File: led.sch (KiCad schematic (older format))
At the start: 2 parts

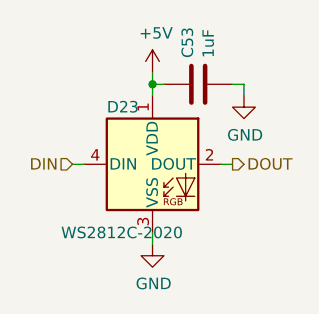
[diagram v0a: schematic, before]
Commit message: Place and route WS2812 LEDs
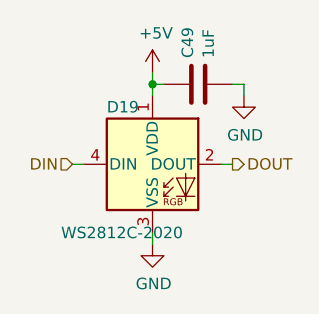
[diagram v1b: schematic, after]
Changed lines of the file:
@@
 $Descr A4 11693 8268
 encoding utf-8
-Sheet 22 23
+Sheet 19 17
 Title ""
 Date ""
@@
 AR Path="/62050786/62063495/6205F43D" Ref="D16"  Part="1"
 AR Path="/62050786/620637A1/6205F43D" Ref="D17"  Part="1"
-F 0 "D23" H 1800 2600 50  0000 L CNN
+F 0 "D19" H 1800 2600 50  0000 L CNN
 F 1 "WS2812C-2020" H 1600 2050 50  0000 L CNN
 F 2 "LED_RGB:LED_RGB_2020_WS2812C" H 2050 2050 50  0001 L TNN
@@
 AR Path="/62050786/62063495/6205F444" Ref="C46"  Part="1"
 AR Path="/62050786/620637A1/6205F444" Ref="C47"  Part="1"
-F 0 "C53" H 2315 2046 50  0000 L CNN
+F 0 "C49" H 2315 2046 50  0000 L CNN
 F 1 "1uF" H 2315 1955 50  0000 L CNN
 F 2 "Capacitor_SMD:C_0402_1005Metric" H 2238 1850 50  0001 C CNN
@@
 AR Path="/62050786/62063495/6205F44A" Ref="#PWR0164"  Part="1"
 AR Path="/62050786/620637A1/6205F44A" Ref="#PWR0167"  Part="1"
-F 0 "#PWR0185" H 2400 1800 50  0001 C CNN
+F 0 "#PWR0173" H 2400 1800 50  0001 C CNN
 F 1 "GND" H 2405 1877 50  0000 C CNN
 F 2 "" H 2400 2050 50  0001 C CNN
@@
 AR Path="/62050786/62063495/6205F452" Ref="#PWR0165"  Part="1"
 AR Path="/62050786/620637A1/6205F452" Ref="#PWR0168"  Part="1"
-F 0 "#PWR0186" H 2000 2450 50  0001 C CNN
+F 0 "#PWR0174" H 2000 2450 50  0001 C CNN
 F 1 "GND" H 2005 2527 50  0000 C CNN
 F 2 "" H 2000 2700 50  0001 C CNN
@@
 AR Path="/62050786/62063495/6205F459" Ref="#PWR0166"  Part="1"
 AR Path="/62050786/620637A1/6205F459" Ref="#PWR0169"  Part="1"
-F 0 "#PWR0187" H 2000 1800 50  0001 C CNN
+F 0 "#PWR0175" H 2000 1800 50  0001 C CNN
 F 1 "+5V" H 2015 2123 50  0000 C CNN
 F 2 "" H 2000 1950 50  0001 C CNN

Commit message: Add option for elevated D-Pad
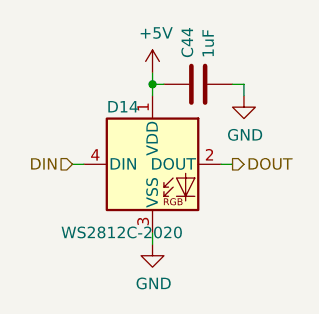
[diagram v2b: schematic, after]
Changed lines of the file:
@@
 $Descr A4 11693 8268
 encoding utf-8
-Sheet 19 17
+Sheet 11 17
 Title ""
 Date ""
@@
 AR Path="/62050786/62063495/6205F43D" Ref="D16"  Part="1"
 AR Path="/62050786/620637A1/6205F43D" Ref="D17"  Part="1"
-F 0 "D19" H 1800 2600 50  0000 L CNN
+F 0 "D14" H 1800 2600 50  0000 L CNN
 F 1 "WS2812C-2020" H 1600 2050 50  0000 L CNN
 F 2 "LED_RGB:LED_RGB_2020_WS2812C" H 2050 2050 50  0001 L TNN
@@
 AR Path="/62050786/62063495/6205F444" Ref="C46"  Part="1"
 AR Path="/62050786/620637A1/6205F444" Ref="C47"  Part="1"
-F 0 "C49" H 2315 2046 50  0000 L CNN
+F 0 "C44" H 2315 2046 50  0000 L CNN
 F 1 "1uF" H 2315 1955 50  0000 L CNN
 F 2 "Capacitor_SMD:C_0402_1005Metric" H 2238 1850 50  0001 C CNN
@@
 AR Path="/62050786/62063495/6205F44A" Ref="#PWR0164"  Part="1"
 AR Path="/62050786/620637A1/6205F44A" Ref="#PWR0167"  Part="1"
-F 0 "#PWR0173" H 2400 1800 50  0001 C CNN
+F 0 "#PWR0158" H 2400 1800 50  0001 C CNN
 F 1 "GND" H 2405 1877 50  0000 C CNN
 F 2 "" H 2400 2050 50  0001 C CNN
@@
 AR Path="/62050786/62063495/6205F452" Ref="#PWR0165"  Part="1"
 AR Path="/62050786/620637A1/6205F452" Ref="#PWR0168"  Part="1"
-F 0 "#PWR0174" H 2000 2450 50  0001 C CNN
+F 0 "#PWR0159" H 2000 2450 50  0001 C CNN
 F 1 "GND" H 2005 2527 50  0000 C CNN
 F 2 "" H 2000 2700 50  0001 C CNN
@@
 AR Path="/62050786/62063495/6205F459" Ref="#PWR0166"  Part="1"
 AR Path="/62050786/620637A1/6205F459" Ref="#PWR0169"  Part="1"
-F 0 "#PWR0175" H 2000 1800 50  0001 C CNN
+F 0 "#PWR0160" H 2000 1800 50  0001 C CNN
 F 1 "+5V" H 2015 2123 50  0000 C CNN
 F 2 "" H 2000 1950 50  0001 C CNN

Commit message: Implement elevated AB surfaces
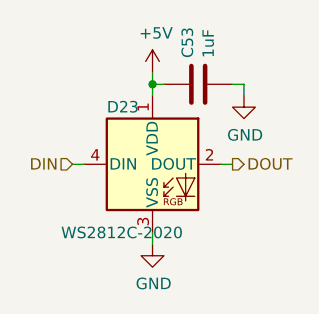
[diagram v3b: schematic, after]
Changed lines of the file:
@@
 AR Path="/62050786/62063495/6205F43D" Ref="D16"  Part="1"
 AR Path="/62050786/620637A1/6205F43D" Ref="D17"  Part="1"
-F 0 "D14" H 1800 2600 50  0000 L CNN
+F 0 "D23" H 1800 2600 50  0000 L CNN
 F 1 "WS2812C-2020" H 1600 2050 50  0000 L CNN
 F 2 "LED_RGB:LED_RGB_2020_WS2812C" H 2050 2050 50  0001 L TNN
@@
 AR Path="/62050786/62063495/6205F444" Ref="C46"  Part="1"
 AR Path="/62050786/620637A1/6205F444" Ref="C47"  Part="1"
-F 0 "C44" H 2315 2046 50  0000 L CNN
+F 0 "C53" H 2315 2046 50  0000 L CNN
 F 1 "1uF" H 2315 1955 50  0000 L CNN
 F 2 "Capacitor_SMD:C_0402_1005Metric" H 2238 1850 50  0001 C CNN
@@
 AR Path="/62050786/62063495/6205F44A" Ref="#PWR0164"  Part="1"
 AR Path="/62050786/620637A1/6205F44A" Ref="#PWR0167"  Part="1"
-F 0 "#PWR0158" H 2400 1800 50  0001 C CNN
+F 0 "#PWR0185" H 2400 1800 50  0001 C CNN
 F 1 "GND" H 2405 1877 50  0000 C CNN
 F 2 "" H 2400 2050 50  0001 C CNN
@@
 AR Path="/62050786/62063495/6205F452" Ref="#PWR0165"  Part="1"
 AR Path="/62050786/620637A1/6205F452" Ref="#PWR0168"  Part="1"
-F 0 "#PWR0159" H 2000 2450 50  0001 C CNN
+F 0 "#PWR0186" H 2000 2450 50  0001 C CNN
 F 1 "GND" H 2005 2527 50  0000 C CNN
 F 2 "" H 2000 2700 50  0001 C CNN
@@
 AR Path="/62050786/62063495/6205F459" Ref="#PWR0166"  Part="1"
 AR Path="/62050786/620637A1/6205F459" Ref="#PWR0169"  Part="1"
-F 0 "#PWR0160" H 2000 1800 50  0001 C CNN
+F 0 "#PWR0187" H 2000 1800 50  0001 C CNN
 F 1 "+5V" H 2015 2123 50  0000 C CNN
 F 2 "" H 2000 1950 50  0001 C CNN
